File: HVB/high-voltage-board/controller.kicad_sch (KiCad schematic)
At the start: 24 parts, among them J10 Conn_01x05, U4 LD1117S33TR_SOT223, U5 STM32F413CGUx, U6 MCP2551-I-SN, Y1 Crystal

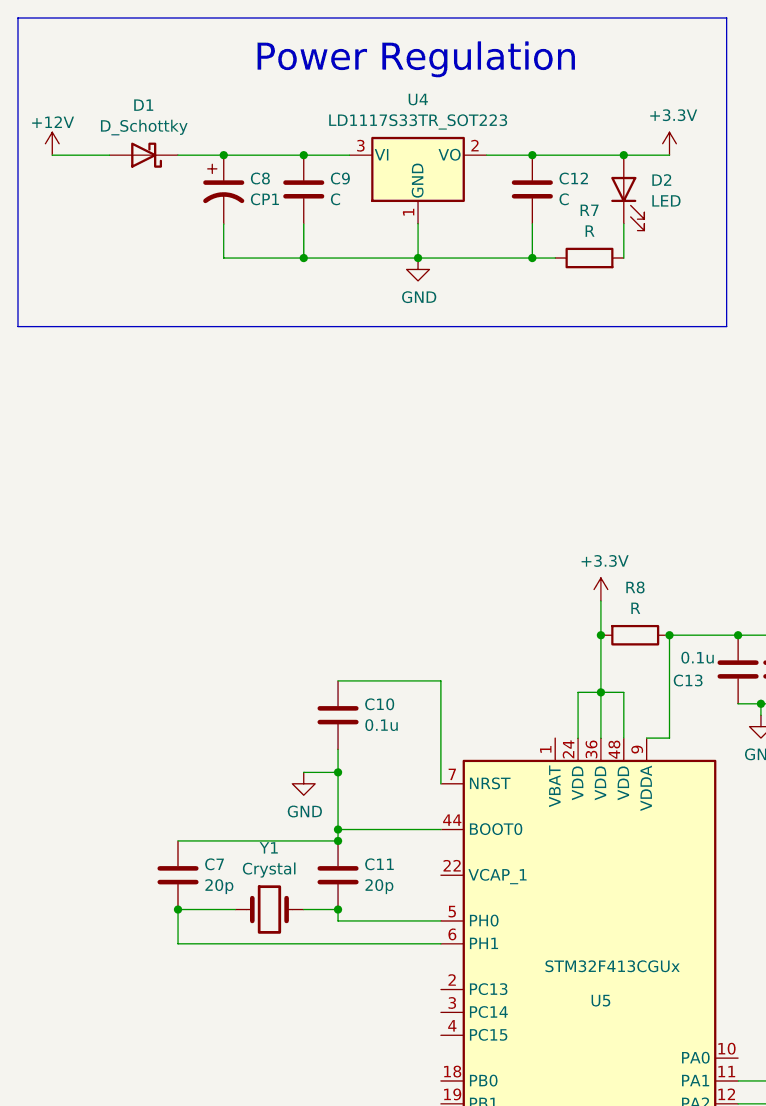
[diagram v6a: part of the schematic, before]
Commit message: updating filtering cap layout
Kay suggested layout changes. Moved caps around
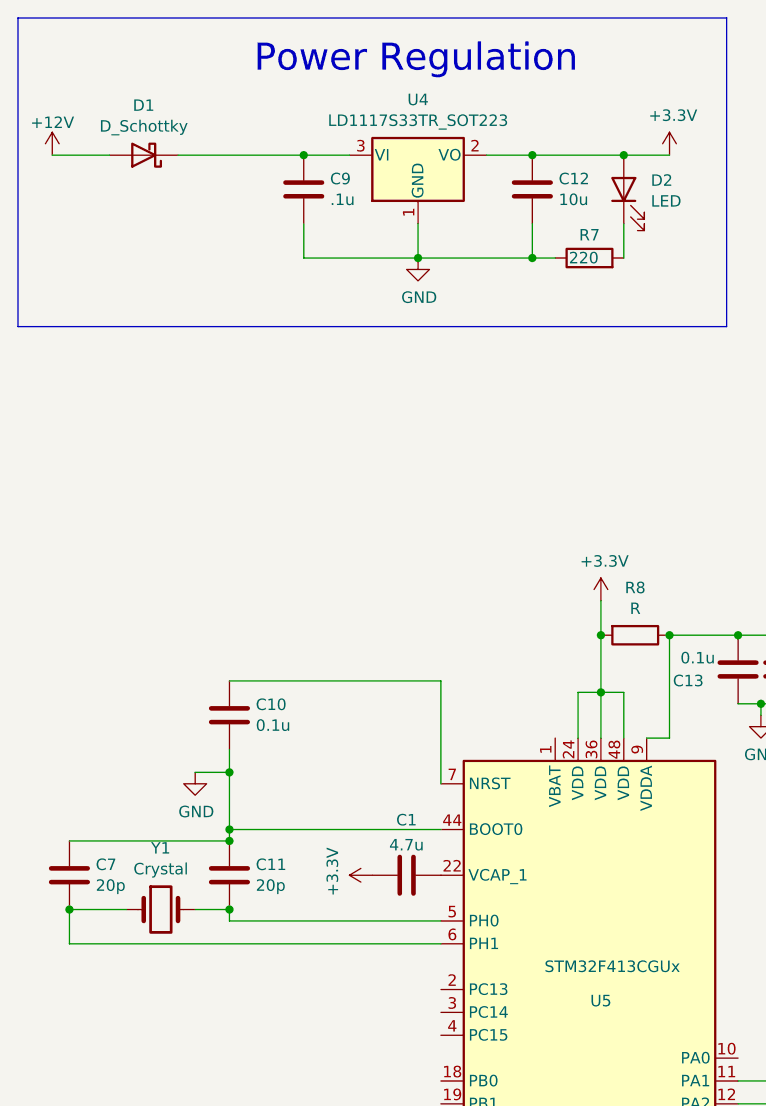
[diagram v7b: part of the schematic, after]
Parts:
- removed C8: CP1, Capacitor_SMD:C_0603_1608Metric_Pad1.08x0.95mm_HandSolder, symbol Device:CP1
- added C1: 4.7u, Capacitor_SMD:C_0603_1608Metric_Pad1.08x0.95mm_HandSolder, symbol Device:C
- C12: value C -> 10u
- C9: value C -> .1u
- R7: value R -> 220
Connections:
- net +3V3: now also C1.1
- net at U5.22 (VCAP_1): now also C1.2
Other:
- moved on the sheet: C10, C11, C7, Y1
